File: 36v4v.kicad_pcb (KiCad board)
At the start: 2 copper layers, 86.3 x 40.5 mm, 34 parts, among them J1 Conn_01x03, J2 Conn_01x02, J3 Conn_01x02, U1 INN3162C-H1XX

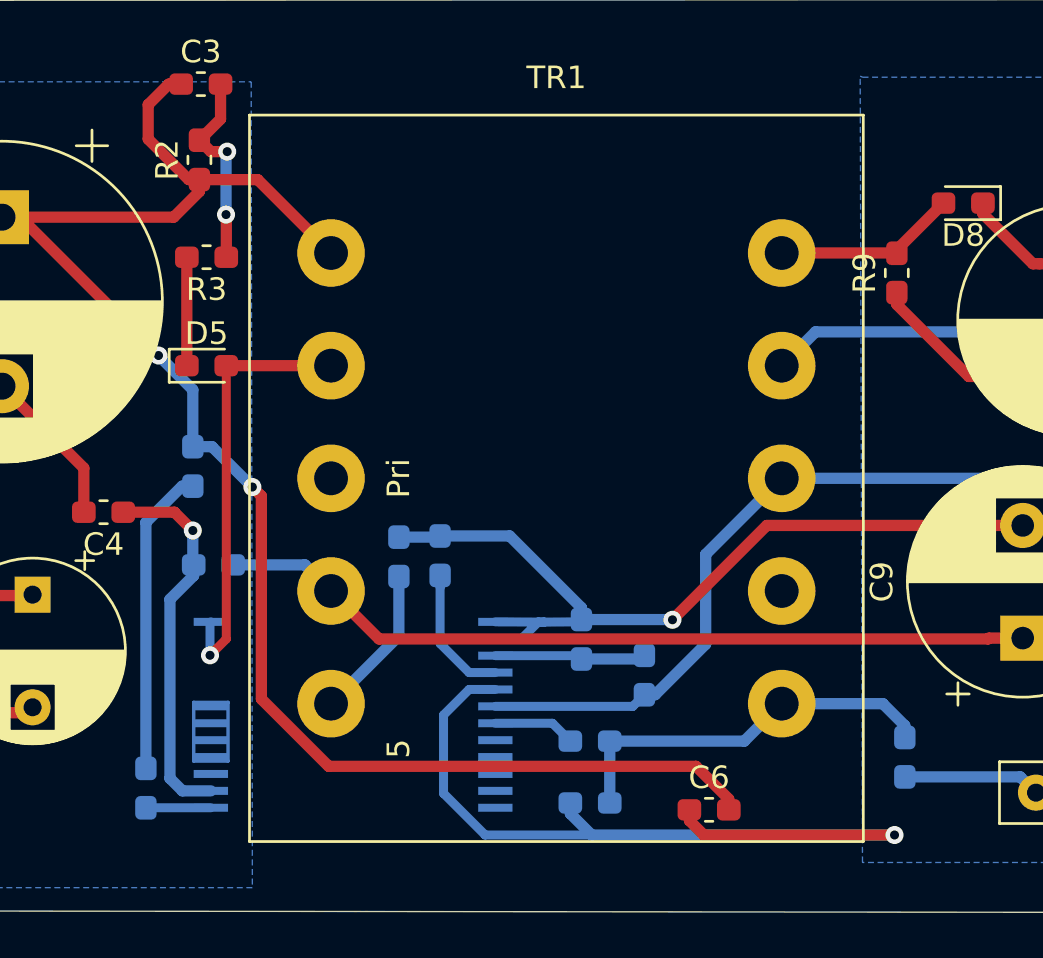
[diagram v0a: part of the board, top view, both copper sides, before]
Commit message: Incorporated Anil's feedback, BOM
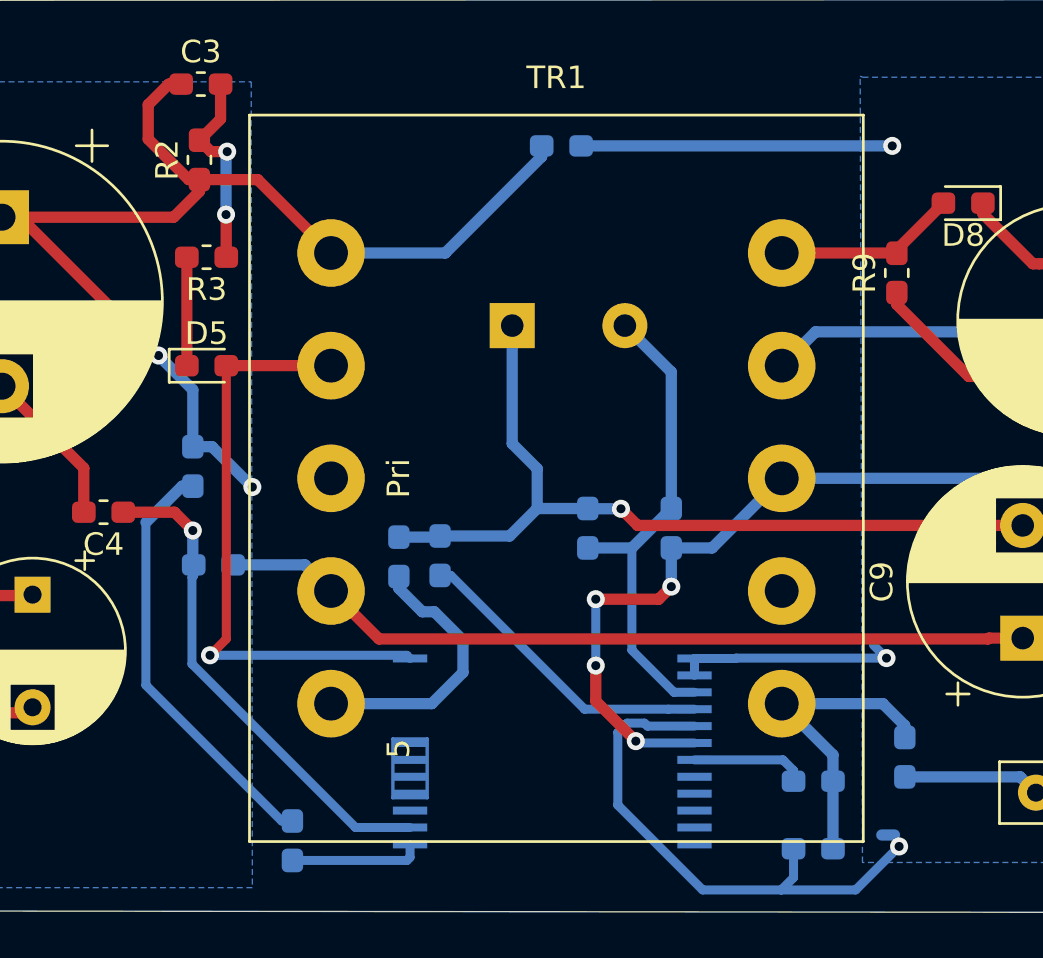
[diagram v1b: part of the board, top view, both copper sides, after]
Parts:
- added C12: 330pF 50V Ceramic, Capacitor_THT:CP_Radial_D10.0mm_P5.00mm, B.Cu at (154.1, 85.7)
- C11: value 22u 50V -> 22u 50V Electrolytic
- C3: value 0.33n 630V -> 0.47n 630V
- C4: value 1u 16V -> 0.47u 16V
- C6: moved to B.Cu
- C8: value 18pF 1KV -> 18pF 1KV Ceramic
- C9: value 22u 35V -> 22u 35V Electrolytic
- D1: value D_Bridge_+AA- -> D_Bridge_+AA- / 800 V, 1 A, Standard Recovery, DO-41
- D6: value D -> 150 V, 0.2 A, Standard Recovery, DO-35
- D7: value D_Zener_Small -> 40 V, 2 A, Schottky, DO-15
- D8: value D -> 400 V, 1 A, Ultrafast Recovery, 30 ns, SOD57
- L1: value L_Core_Ferrite_Coupled -> 1 mH, 0.18 A
- R1: value 4.7K -> 4.7 kΩ, 5 %, 0.25 W, Carbon Film
- R10: value 80.6K 1% -> 80.6 kΩ, 1 %, 0.125 W, Metal Film
- R11: value 29.4K 1% -> 29.4 kΩ, 1 %, 0.125 W, Metal Film
- R2: value 240K -> 240 kΩ, 5 %, 0.25 W, Carbon Film
- R3: value 43 -> 43 Ω, 5 %, 0.125 W, Carbon Film
- R4, R5: value 1.78M 1% -> 1.78 MΩ, 1 %, 0.25 W, Metal Film
- R6: value 14K 1% -> 14 kΩ, 1 %, 0.125 W, Metal Film
- R7: value 47 -> 47 Ω, 5 %, 0.125 W, Carbon Film
- R8: value 22 -> 22 Ω, 5 %, 0.25 W, Carbon Film
- R9: value 560 -> 560 Ω, 5 %, 0.25 W, Carbon Film
- RF1: value 10 2W -> 10 Ω, 2 W, Flameproof Wire-Wound Resistor
- U1: value INN3162C-H1XX -> InnoSwitch3-CE, INN3162C, inSOP-24D
- moved C6 30.2 mm to (156.3, 77.7), turned to 180 degrees
- moved D7 10.1 mm to (167.5, 108.9)
- moved R7 10.1 mm to (167.5, 105.9)
- moved U1 8.99 mm to (155.9, 104.6)
- moved R5 6.91 mm to (144.4, 108.6)
- moved R10 6.62 mm to (161.2, 94.7)
- moved R11 4.94 mm to (157.5, 94.7)
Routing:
- net Net-(C2-Pad1): track 84.5 -> 63.4 mm
- net Net-(C12-Pad2): track 6.74 -> 21.5 mm
- net GND: track 76.3 -> 85.3 mm, vias 2 -> 4
- net Net-(C5-Pad2): track 6.01 -> 13.7 mm
- net Net-(D5-Pad2): track 19.3 -> 26.7 mm
- net Net-(R4-Pad1): track 13.7 -> 19.0 mm
- net Net-(D6-Pad1): track 6.89 -> 12.2 mm
- net Net-(C4-Pad1): track 16.9 -> 22.1 mm
- net Net-(D7-Pad1): track 17.5 -> 13.8 mm
- net Net-(R5-Pad1): track 2.88 -> 5.85 mm
- net /4V: track 57.8 -> 59.7 mm, vias 0 -> 4
- net Net-(R7-Pad1): track 3.66 -> 5.07 mm

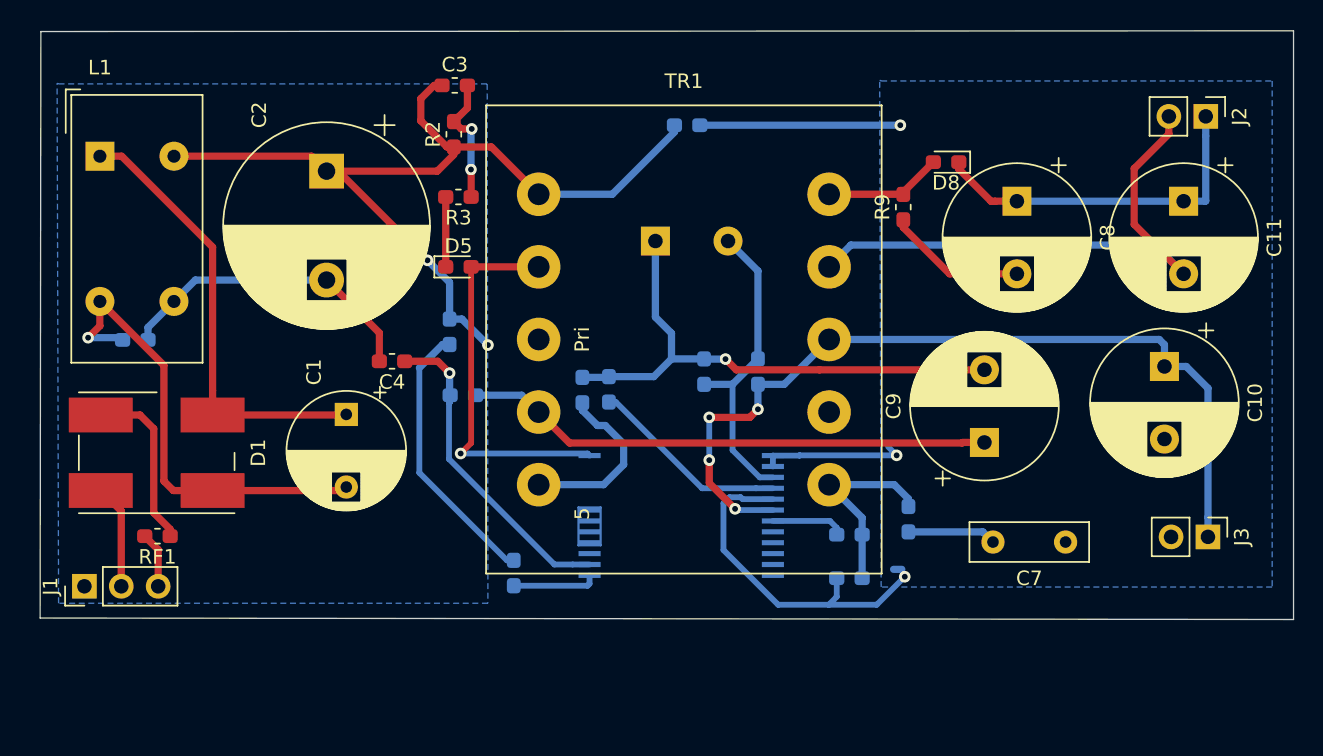
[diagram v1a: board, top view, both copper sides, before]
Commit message: Changed cap footprints, layout. Added datasheets
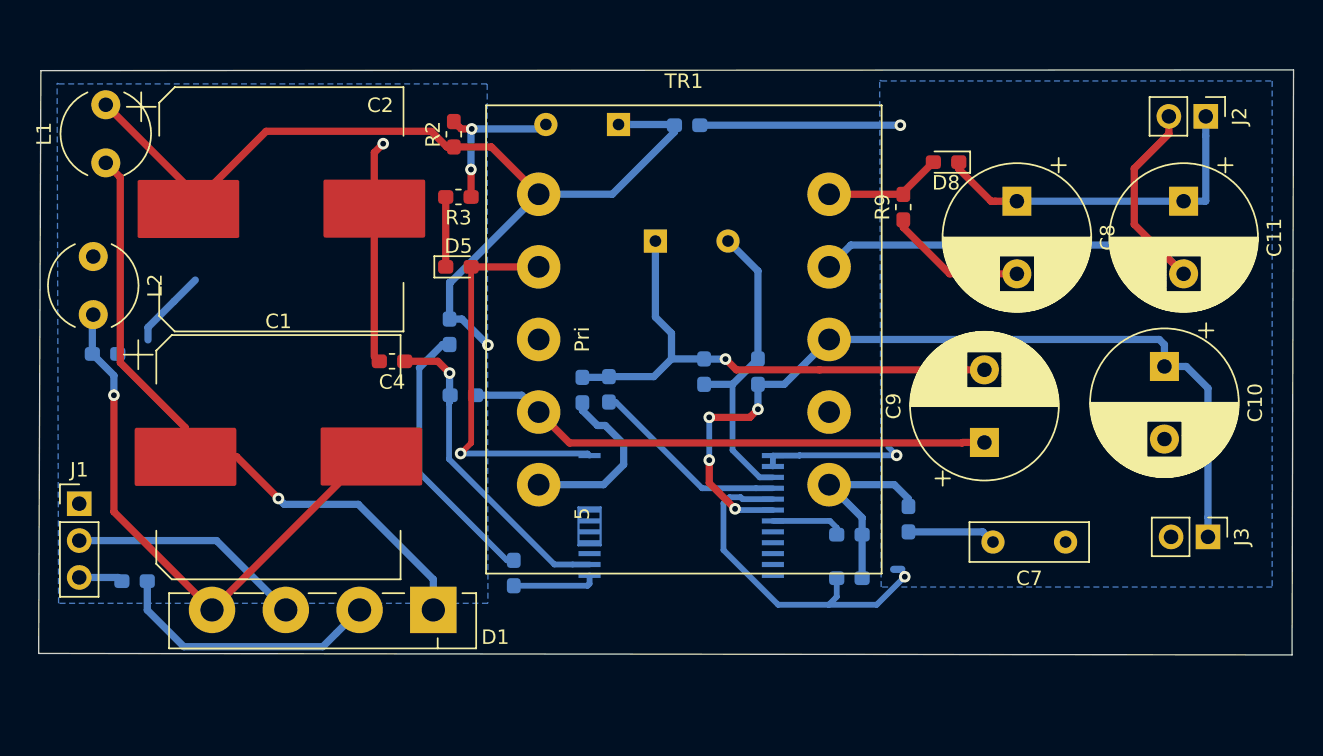
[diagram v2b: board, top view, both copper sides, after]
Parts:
- added L2: L, Inductor_THT:L_Radial_D6.0mm_P4.00mm, F.Cu at (115.4, 86.8)
- C1: footprint Capacitor_THT:CP_Radial_D8.0mm_P5.00mm -> pwrcon:CP_Elec_EEV_16x17.5
- C12: footprint Capacitor_THT:CP_Radial_D10.0mm_P5.00mm -> Capacitor_THT:CP_Radial_D8.0mm_P5.00mm
- C2: footprint Capacitor_THT:CP_Radial_D14.0mm_P7.50mm -> pwrcon:CP_Elec_EEV_16x17.5
- C3: footprint Capacitor_SMD:C_0603_1608Metric_Pad1.05x0.95mm_HandSolder -> Capacitor_THT:CP_Radial_Tantal_D5.5mm_P5.00mm; moved to B.Cu
- D1: footprint Diode_SMD:Diode_Bridge_Bourns_CD-DF4xxS -> Diode_THT:Diode_Bridge_Vishay_GBL
- L1: value 1 mH, 0.18 A -> L; footprint Inductor_THT:Choke_Schaffner_RN202-04-8.8x18.2mm -> Inductor_THT:L_Radial_D6.0mm_P4.00mm
- RF1: moved to B.Cu
- moved D1 21.9 mm to (138.8, 111.1), turned to 180 degrees
- moved C3 11.6 mm to (151.6, 77.7), turned to 180 degrees
- moved J1 5.70 mm to (114.5, 103.8), turned to 0 degrees
- moved C1 5.52 mm to (128.2, 100.6), turned to 0 degrees
- moved C2 4.07 mm to (128.4, 83.5), turned to 0 degrees
- moved RF1 3.48 mm to (118.3, 109.1)
- moved R1 2.30 mm to (116.2, 93.5)
- moved L1 0.61 mm to (116.3, 80.3), turned to 90 degrees
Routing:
- net Net-(C1-Pad1): track 31.1 -> 45.2 mm, vias 0 -> 1
- net Net-(D1-Pad3): track 7.18 -> 16.2 mm
- net Net-(D1-Pad2): track 11.9 -> 18.7 mm
- net Net-(C1-Pad2): track 32.4 -> 39.1 mm
- net Net-(C2-Pad1): track 63.4 -> 67.7 mm, vias 2 -> 1
- net Net-(C3-Pad2): track 9.03 -> 11.4 mm
- net Net-(J1-Pad3): track 3.84 -> 3.04 mm
- net Earth: track 21.6 -> 20.9 mm, vias 0 -> 1
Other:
- board size 86.3 x 40.5 mm -> 86.4 x 40.3 mm

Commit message: Changed pcz size, modified footprints
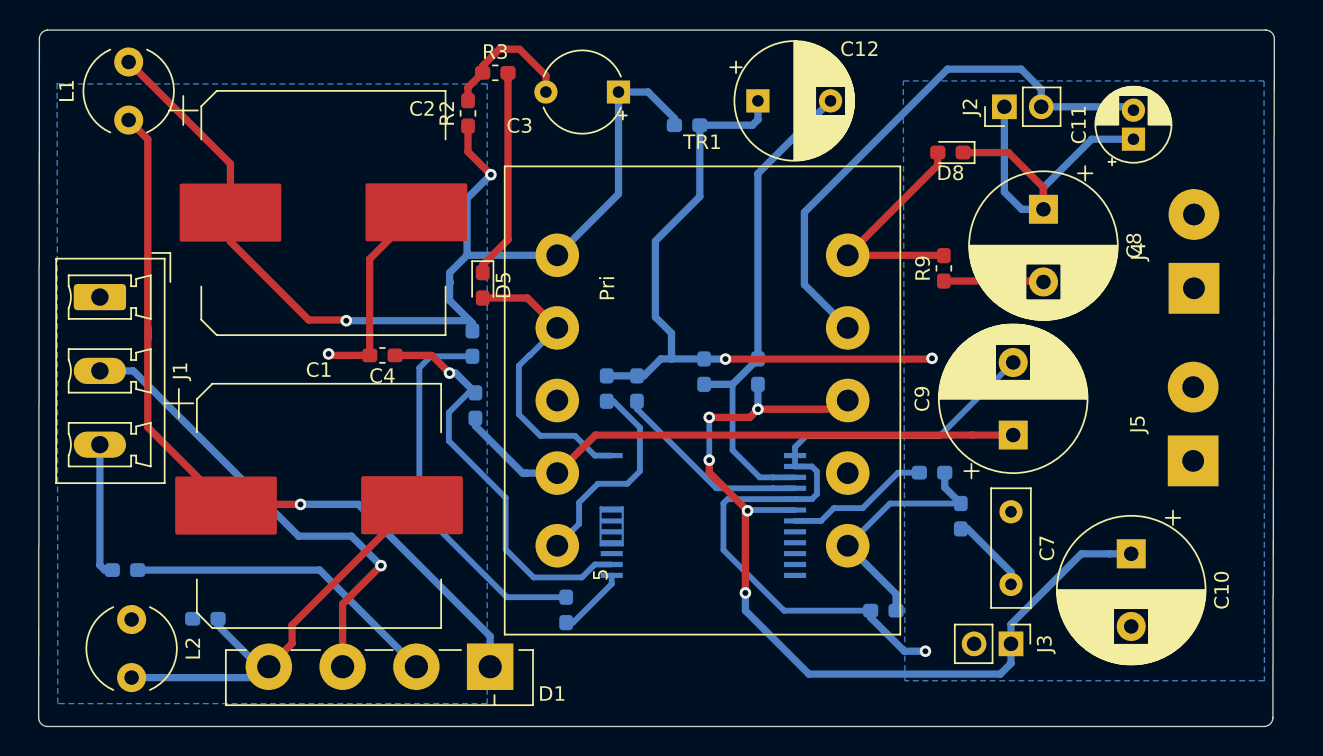
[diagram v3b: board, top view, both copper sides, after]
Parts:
- added J4: Conn_01x02, Connector_Wire:SolderWirePad_1x02_P5.08mm_Drill1.5mm, F.Cu at (191.2, 89.0)
- added J5: Conn_01x02, Connector_Wire:SolderWirePad_1x02_P5.08mm_Drill1.5mm, F.Cu at (191.2, 100.8)
- C11: footprint Capacitor_THT:CP_Radial_D10.0mm_P5.00mm -> Capacitor_THT:CP_Radial_D5.0mm_P2.00mm
- C12, C3: moved to F.Cu
- J1: footprint Connector_PinHeader_2.54mm:PinHeader_1x03_P2.54mm_Vertical -> Connector_Phoenix_MC_HighVoltage:PhoenixContact_MCV_1,5_3-G-5.08_1x03_P5.08mm_Vertical
- moved L2 25.1 mm to (118.1, 111.8)
- moved R1 19.5 mm to (123.1, 111.7), turned to 0 degrees
- moved J3 15.4 mm to (178.6, 113.4)
- moved J1 14.3 mm to (115.9, 89.6), turned to 270 degrees
- moved J2 13.9 mm to (178.2, 76.5), turned to 90 degrees
- moved C10 13.1 mm to (186.9, 107.2)
- moved C12 12.0 mm to (161.2, 76.0)
- moved R3 8.92 mm to (143.1, 74.1), turned to 0 degrees
- moved R7 7.11 mm to (173.2, 101.7)
- moved D1 5.53 mm to (142.7, 115.0)
- moved C11 5.49 mm to (187.0, 78.7), turned to 90 degrees
- moved R9 5.06 mm to (174.0, 87.6)
- moved R5 4.41 mm to (148.0, 111.1)
- moved TR1 4.40 mm to (147.4, 106.7)
- moved C1 4.36 mm to (131.0, 103.9)
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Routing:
- net Net-(D1-Pad3): track 16.2 -> 33.0 mm, vias 0 -> 1
- net Net-(C12-Pad2): track 21.5 -> 33.9 mm
- net GND: track 85.3 -> 95.2 mm, vias 4 -> 3
- net Net-(D5-Pad1): track 4.81 -> 14.5 mm
- net Net-(C1-Pad2): track 39.1 -> 30.1 mm, vias 1 -> 0
- net Net-(C1-Pad1): track 45.2 -> 53.4 mm
- net Net-(D8-Pad2): track 8.19 -> 16.3 mm
- net Net-(R4-Pad1): track 19.0 -> 26.4 mm
- net Net-(C2-Pad1): track 67.7 -> 75.0 mm, vias 1 -> 2
- net Net-(C4-Pad1): track 22.1 -> 28.5 mm
- net Net-(J1-Pad3): track 3.04 -> 9.30 mm
- net Net-(D5-Pad2): track 26.7 -> 20.6 mm, vias 1 -> 0
- net Earth: track 20.9 -> 14.9 mm
- net Net-(R7-Pad1): track 5.07 -> 9.94 mm
- net Net-(D7-Pad1): track 13.8 -> 17.4 mm
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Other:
- board size 86.4 x 40.3 mm -> 85.1 x 48 mm

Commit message: Changes to components and footprints as suggested by AA
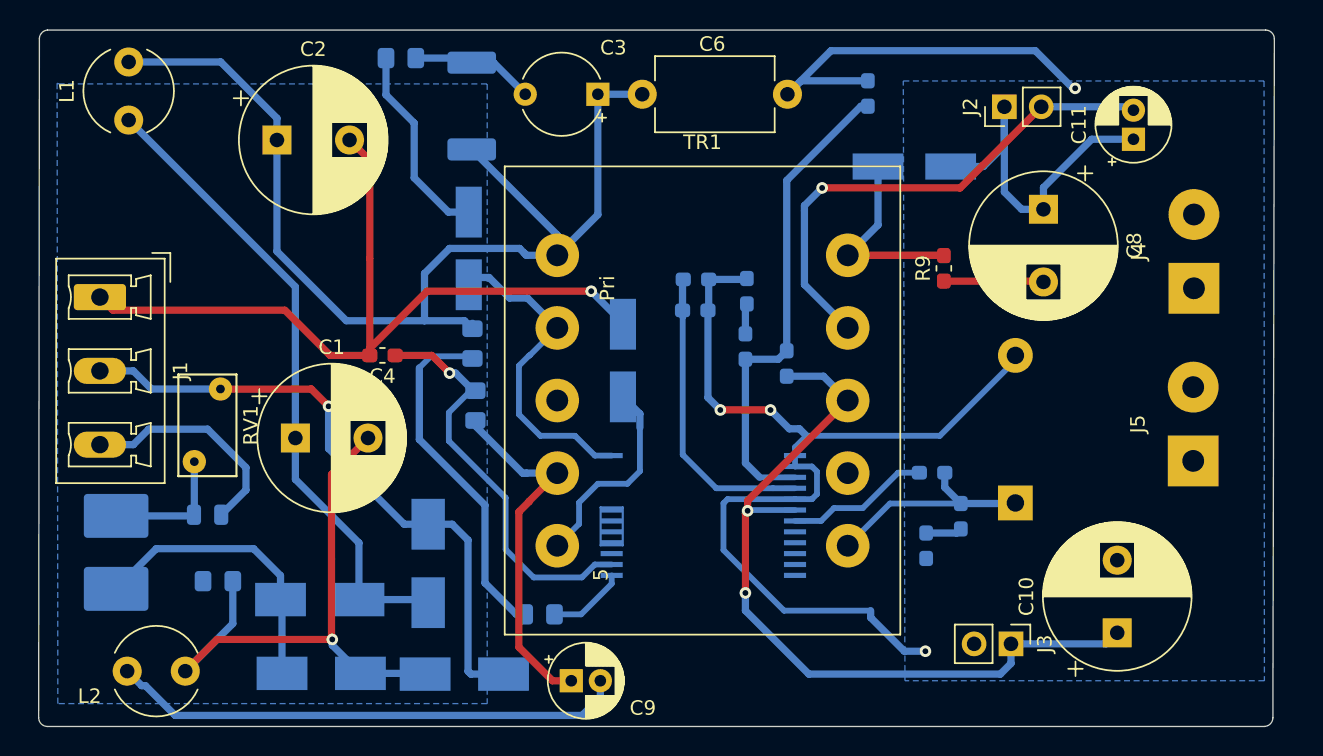
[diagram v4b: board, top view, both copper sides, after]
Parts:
- added C5A1: 2.2u 50V, Capacitor_SMD:C_0603_1608Metric_Pad1.05x0.95mm_HandSolder, B.Cu at (156.9, 88.3)
- added D2: D_Small, Diode_SMD:D_SMB_Handsoldering, B.Cu at (131.1, 115.5)
- added D3: D_Small, Diode_SMD:D_SMB_Handsoldering, B.Cu at (138.5, 107.9)
- added D4: D_Small, Diode_SMD:D_SMB_Handsoldering, B.Cu at (141.0, 115.5)
- added F1: Fuse_Small, Fuse:Fuse_0805_2012Metric, B.Cu at (123.3, 104.5)
- added R11b1: 29.4 kΩ, 1 %, 0.125 W, Metal Film, Resistor_SMD:R_0603_1608Metric_Pad1.05x0.95mm_HandSolder, B.Cu at (160.4, 89.2)
- added RV1: Varistor, Varistor:RV_Disc_D7mm_W4mm_P5mm, F.Cu at (122.4, 100.9)
- C1, C2: footprint pwrcon:CP_Elec_EEV_16x17.5 -> Capacitor_THT:CP_Radial_D10.0mm_P5.00mm
- C12: footprint Capacitor_THT:CP_Radial_D8.0mm_P5.00mm -> Capacitor_SMD:C_0603_1608Metric_Pad1.05x0.95mm_HandSolder; moved to B.Cu
- C6: footprint Capacitor_SMD:C_0603_1608Metric_Pad1.05x0.95mm_HandSolder -> Capacitor_THT:C_Disc_D8.0mm_W5.0mm_P10.00mm; moved to F.Cu
- C7: footprint Capacitor_THT:C_Disc_D8.0mm_W2.5mm_P5.00mm -> Capacitor_SMD:C_0603_1608Metric_Pad1.05x0.95mm_HandSolder; moved to B.Cu
- C9: footprint Capacitor_THT:CP_Radial_D10.0mm_P5.00mm -> Capacitor_THT:CP_Radial_D5.0mm_P2.00mm
- D1: value D_Bridge_+AA- / 800 V, 1 A, Standard Recovery, DO-41 -> D_Small; footprint Diode_THT:Diode_Bridge_Vishay_GBL -> Diode_SMD:D_SMB_Handsoldering; moved to B.Cu
- D5, D8: footprint Diode_SMD:D_0603_1608Metric_Pad1.05x0.95mm_HandSolder -> Diode_SMD:D_SMA_Handsoldering; moved to B.Cu
- D6: footprint Diode_SMD:D_0603_1608Metric_Pad1.05x0.95mm_HandSolder -> Diode_SMD:D_SMA_Handsoldering
- D7: footprint Diode_SMD:D_0603_1608Metric_Pad1.05x0.95mm_HandSolder -> Diode_THT:D_DO-15_P10.16mm_Horizontal
- R1, R4, R5, R6: footprint Resistor_SMD:R_0603_1608Metric_Pad1.05x0.95mm_HandSolder -> Resistor_SMD:R_0805_2012Metric_Pad1.15x1.40mm_HandSolder
- R2: footprint Resistor_SMD:R_0603_1608Metric_Pad1.05x0.95mm_HandSolder -> Resistor_SMD:R_2512_6332Metric_Pad1.52x3.35mm_HandSolder; moved to B.Cu
- R3: footprint Resistor_SMD:R_0603_1608Metric_Pad1.05x0.95mm_HandSolder -> Resistor_SMD:R_0805_2012Metric_Pad1.15x1.40mm_HandSolder; moved to B.Cu
- RF1: footprint Resistor_SMD:R_0603_1608Metric_Pad1.05x0.95mm_HandSolder -> Resistor_SMD:R_2816_7142Metric
- moved C9 34.8 mm to (148.3, 116.0), turned to 0 degrees
- moved D1 12.6 mm to (131.0, 110.4)
- moved D7 11.7 mm to (178.9, 103.7), turned to 90 degrees
- moved C12 7.59 mm to (168.8, 75.5), turned to 270 degrees
- moved C6 7.23 mm to (163.2, 75.6)
- moved C5 6.72 mm to (156.9, 90.5), turned to 180 degrees
- moved R3 6.58 mm to (136.6, 73.1), turned to 180 degrees
- moved C7 6.29 mm to (172.8, 106.7), turned to 90 degrees
- moved C2 5.96 mm to (128.1, 78.7)
- moved C10 5.52 mm to (185.9, 112.7), turned to 90 degrees
- moved C1 4.95 mm to (129.3, 99.3)
- moved L2 3.57 mm to (117.8, 115.3), turned to 0 degrees
- moved R11a1 3.33 mm to (160.3, 93.0)
- moved R1 2.73 mm to (124.0, 109.1)
- moved D5 2.72 mm to (141.3, 86.2)
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- renumbered R11 to R11a1
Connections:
- C9 pad 2: GND -> Earth
- D6 pad 2: GND -> Earth
- J1 pad 1: (no net) -> Earth
- J1 pad 2: Net-(D1-Pad3) -> Net-(D3-Pad2)
- J1 pad 3: Net-(J1-Pad3) -> Net-(F1-Pad1)
- R11a1 pad 1: GND -> Net-(R11a1-Pad1)
- RF1 pad 2: Net-(J1-Pad3) -> Net-(F1-Pad2)
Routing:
- net Earth: track 14.9 -> 91.7 mm
- net Net-(D3-Pad2): track 0.00 -> 43.4 mm, vias 0 -> 1
- net Net-(D1-Pad3): track 33.0 -> 0.00 mm, vias 1 -> 0
- net Net-(F1-Pad1): track 0.00 -> 15.6 mm
- net Net-(C9-Pad1): track 40.0 -> 25.2 mm
- net Net-(C1-Pad2): track 30.1 -> 41.1 mm, vias 0 -> 1
- net Net-(F1-Pad2): track 0.00 -> 10.7 mm
- net Net-(J1-Pad3): track 9.30 -> 0.00 mm
- net Net-(C1-Pad1): track 53.4 -> 44.4 mm, vias 1 -> 0
- net Net-(C5-Pad2): track 13.7 -> 20.8 mm
- net /4V: track 62.9 -> 55.8 mm, vias 5 -> 2
- net Net-(C7-Pad2): track 5.53 -> 2.50 mm
- net Net-(D8-Pad2): track 16.3 -> 13.6 mm
- net /GND1: track 37.8 -> 35.2 mm, vias 0 -> 1
- net Net-(R11a1-Pad1): track 0.00 -> 2.10 mm
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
